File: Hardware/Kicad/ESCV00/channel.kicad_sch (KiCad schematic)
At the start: 45 parts, among them Q101 BSZ018N04LS6, Q102 BSZ018N04LS6, Q103 BSZ018N04LS6, Q104 BSZ018N04LS6, Q105 BSZ018N04LS6, Q106 BSZ018N04LS6, U101 STM32F051K8U6, U102 DRV8300DRGER

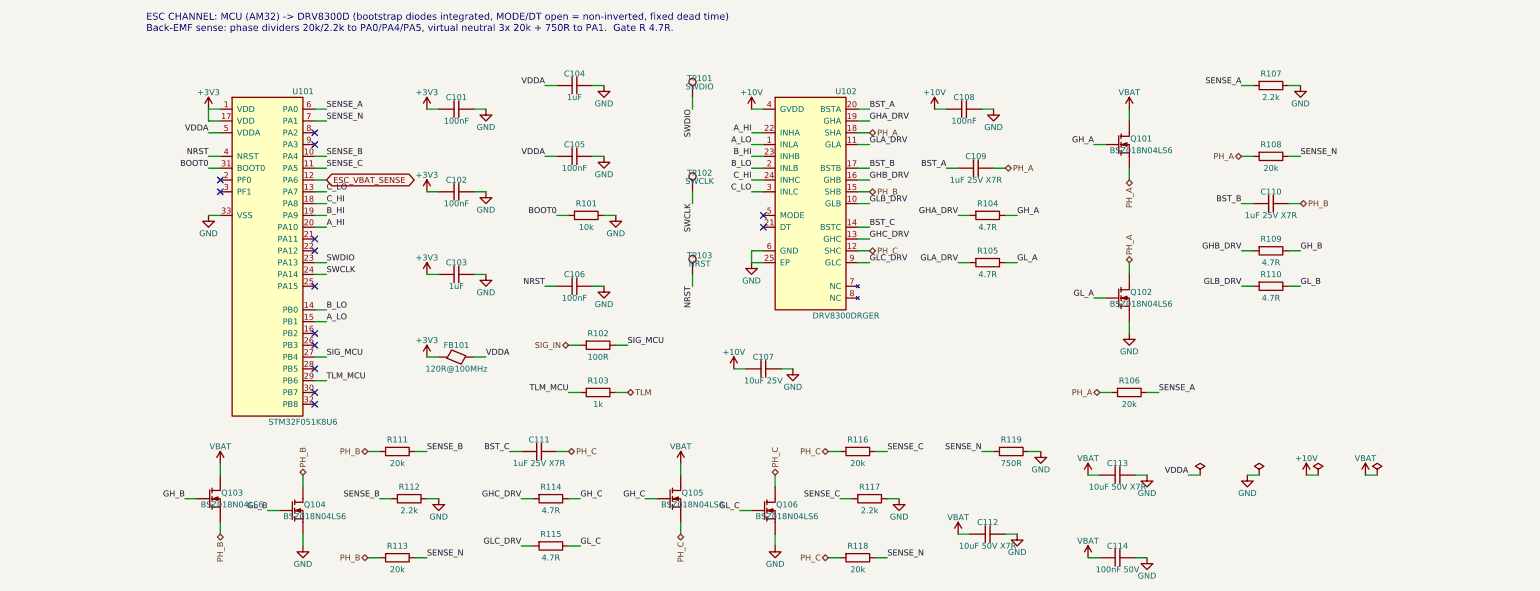
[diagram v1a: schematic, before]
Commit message: Boards follow the B0_EE part convention
- every real part uses the symbol/footprint/3D/datasheet named after its MPN in Kicad_Libs
- symbols keep only Reference, Value, Footprint, Datasheet, Description
  (MPN, Manufacturer, Verify, LCSC, Note fields removed; Verify notes moved to the Readme)
- schematic symbol caches rebuilt from the libraries, PCB footprints relinked with the
  same fields and 3D models as the library (connectivity unchanged)
- DNP and BOM attributes of the footprints match the symbols
- BOMs re-exported with kicad-cli
- ignore KiCad local history
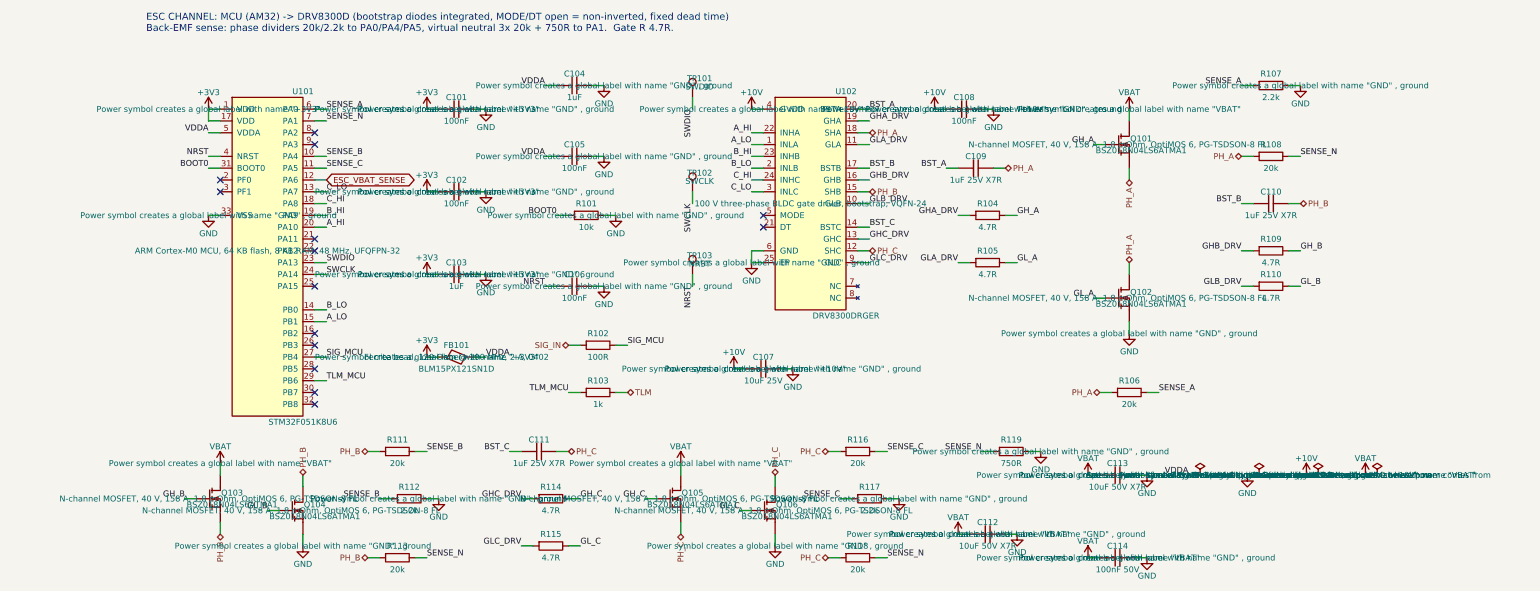
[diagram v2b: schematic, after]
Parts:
- FB101: value 120R@100MHz -> BLM15PX121SN1D; footprint eChoke:L_0402_1005Metric -> eFerrite:BLM15PX121SN1D; symbol eChoke:FB -> eFerrite:BLM15PX121SN1D; MPN BLM15PX121SN1D -> (none)
- Q101, Q102, Q103, Q104, Q105, Q106: value BSZ018N04LS6 -> BSZ018N04LS6ATMA1; footprint eTransistor:PQFN-8_3.3x3.3mm_P0.65mm_PowerFET -> eTransistor:BSZ018N04LS6ATMA1; symbol eTransistor:BSZ018N04LS6 -> eTransistor:BSZ018N04LS6ATMA1; MPN BSZ018N04LS6ATMA1 -> (none); Manufacturer Infineon -> (none); Verify Land pattern copied from TI NexFET SON3.3 (same S-S-S-G / D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 -> (none)
- TP101, TP102, TP103: now left out of the parts list
- U101: footprint eMCU:QFN-32-1EP_5x5mm_P0.5mm_EP3.45x3.45mm -> eMCU:STM32F051K8U6; MPN STM32F051K8U6 -> (none); Manufacturer STMicroelectronics -> (none)
- U102: footprint eInterface:VQFN-24-1EP_4x4mm_P0.5mm_EP2.45x2.45mm -> eInterface:DRV8300DRGER; MPN DRV8300DRGER -> (none); Manufacturer Texas Instruments -> (none); Verify Pin table typed from TI DRV8300 datasheet (RGE pin table). 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 -> (none)

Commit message: Cleared all the descriptions and started Power section for FCV
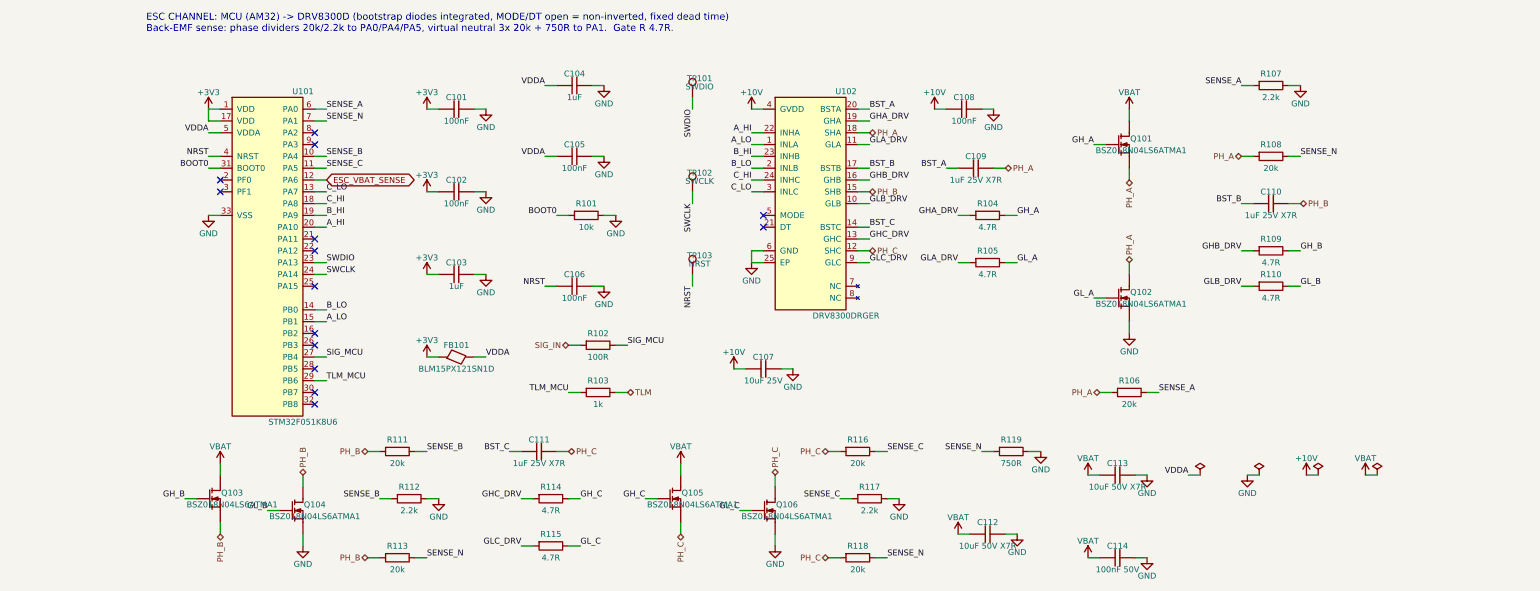
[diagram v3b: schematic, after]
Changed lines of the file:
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@@
 			(show_name no)
 			(do_not_autoplace no)
+			(hide yes)
 			(effects
 				(font
@@
 			(show_name no)
 			(do_not_autoplace no)
+			(hide yes)
 			(effects
 				(font
@@
 			(show_name no)
 			(do_not_autoplace no)
+			(hide yes)
 			(effects
 				(font
@@
 			(show_name no)
 			(do_not_autoplace no)
+			(hide yes)
 			(effects
 				(font
@@
 			(show_name no)
 			(do_not_autoplace no)
+			(hide yes)
 			(effects
 				(font
@@
 			(show_name no)
 			(do_not_autoplace no)
+			(hide yes)
 			(effects
 				(font
@@
 			(show_name no)
 			(do_not_autoplace no)
+			(hide yes)
 			(effects
 				(font
@@
 			(show_name no)
 			(do_not_autoplace no)
+			(hide yes)
 			(effects
 				(font
@@
 			(show_name no)
 			(do_not_autoplace no)
+			(hide yes)
 			(effects
 				(font
@@
 			(show_name no)
 			(do_not_autoplace no)
+			(hide yes)
 			(effects
 				(font
@@
 			(show_name no)
 			(do_not_autoplace no)
+			(hide yes)
 			(effects
 				(font
@@
 			(show_name no)
 			(do_not_autoplace no)
+			(hide yes)
 			(effects
 				(font
@@
 			(show_name no)
 			(do_not_autoplace no)
+			(hide yes)
 			(effects
 				(font
@@
 			(show_name no)
 			(do_not_autoplace no)
+			(hide yes)
 			(effects
 				(font
@@
 			(show_name no)
 			(do_not_autoplace no)
+			(hide yes)
 			(effects
 				(font
@@
 			(show_name no)
 			(do_not_autoplace no)
+			(hide yes)
 			(effects
 				(font
@@
 			(show_name no)
 			(do_not_autoplace no)
+			(hide yes)
 			(effects
 				(font
@@
 			(show_name no)
 			(do_not_autoplace no)
+			(hide yes)
 			(effects
 				(font
@@
 			(show_name no)
 			(do_not_autoplace no)
+			(hide yes)
 			(effects
 				(font
@@
 			(show_name no)
 			(do_not_autoplace no)
+			(hide yes)
 			(effects
 				(font
@@
 			(show_name no)
 			(do_not_autoplace no)
+			(hide yes)
 			(effects
 				(font
@@
 			(show_name no)
 			(do_not_autoplace no)
+			(hide yes)
 			(effects
 				(font
@@
 			(show_name no)
 			(do_not_autoplace no)
+			(hide yes)
 			(effects
 				(font
@@
 			(show_name no)
 			(do_not_autoplace no)
+			(hide yes)
 			(effects
 				(font
@@
 			(show_name no)
 			(do_not_autoplace no)
+			(hide yes)
 			(effects
 				(font
@@
 			(show_name no)
 			(do_not_autoplace no)
+			(hide yes)
 			(effects
 				(font
@@
 			(show_name no)
 			(do_not_autoplace no)
+			(hide yes)
 			(effects
 				(font
@@
 			(show_name no)
 			(do_not_autoplace no)
+			(hide yes)
 			(effects
 				(font
@@
 			(show_name no)
 			(do_not_autoplace no)
+			(hide yes)
 			(effects
 				(font
@@
 			(show_name no)
 			(do_not_autoplace no)
+			(hide yes)
 			(effects
 				(font
@@
 			(show_name no)
 			(do_not_autoplace no)
+			(hide yes)
 			(effects
 				(font
@@
 			(show_name no)
 			(do_not_autoplace no)
+			(hide yes)
 			(effects
 				(font
@@
 			(show_name no)
 			(do_not_autoplace no)
+			(hide yes)
 			(effects
 				(font
@@
 			(show_name no)
 			(do_not_autoplace no)
+			(hide yes)
 			(effects
 				(font
@@
 			(show_name no)
 			(do_not_autoplace no)
+			(hide yes)
 			(effects
 				(font
@@
 			(show_name no)
 			(do_not_autoplace no)
+			(hide yes)
 			(effects
 				(font
@@
 			(show_name no)
 			(do_not_autoplace no)
+			(hide yes)
 			(effects
 				(font
@@
 			(show_name no)
 			(do_not_autoplace no)
+			(hide yes)
 			(effects
 				(font
@@
 			(show_name no)
 			(do_not_autoplace no)
+			(hide yes)
 			(effects
 				(font
@@
 			(show_name no)
 			(do_not_autoplace no)
+			(hide yes)
 			(effects
 				(font
@@
 			(show_name no)
 			(do_not_autoplace no)
+			(hide yes)
 			(effects
 				(font
@@
 			(show_name no)
 			(do_not_autoplace no)
+			(hide yes)
 			(effects
 				(font
@@
 			(show_name no)
 			(do_not_autoplace no)
+			(hide yes)
 			(effects
 				(font
@@
 			(show_name no)
 			(do_not_autoplace no)
+			(hide yes)
 			(effects
 				(font
@@
 			(show_name no)
 			(do_not_autoplace no)
+			(hide yes)
 			(effects
 				(font
@@
 			(show_name no)
 			(do_not_autoplace no)
+			(hide yes)
 			(effects
 				(font
@@
 			(show_name no)
 			(do_not_autoplace no)
+			(hide yes)
 			(effects
 				(font
@@
 			(show_name no)
 			(do_not_autoplace no)
+			(hide yes)
 			(effects
 				(font
@@
 			(show_name no)
 			(do_not_autoplace no)
+			(hide yes)
 			(effects
 				(font
@@
 			(show_name no)
 			(do_not_autoplace no)
+			(hide yes)
 			(effects
 				(font
@@
 			(show_name no)
 			(do_not_autoplace no)
+			(hide yes)
 			(effects
 				(font
